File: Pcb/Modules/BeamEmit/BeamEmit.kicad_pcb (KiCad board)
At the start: 2 copper layers, 50.8 x 20.3 mm, 14 parts, among them J1 JACK_RJ45, Q1 Q_NMOS_GSD, X1 HOLE, X2 HOLE, X3 HOLE, X4 HOLE

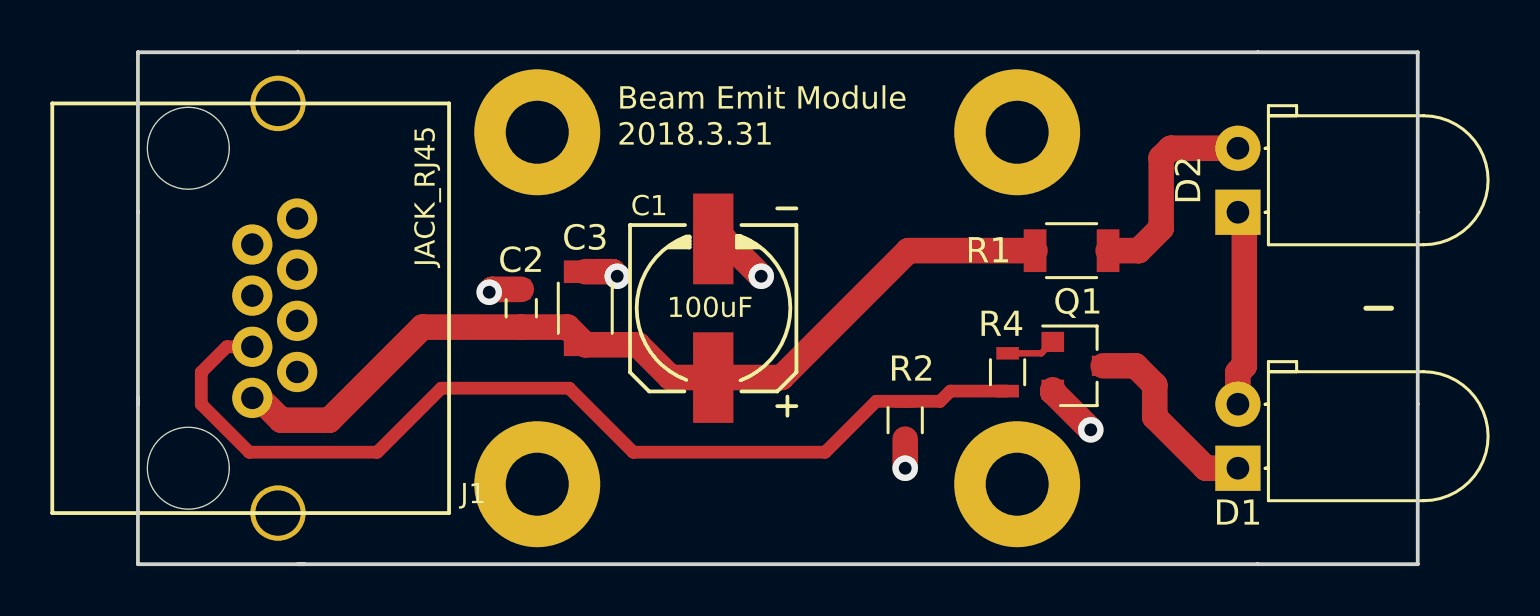
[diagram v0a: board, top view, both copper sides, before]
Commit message: Update module pcbs to fix minor issues and round corners
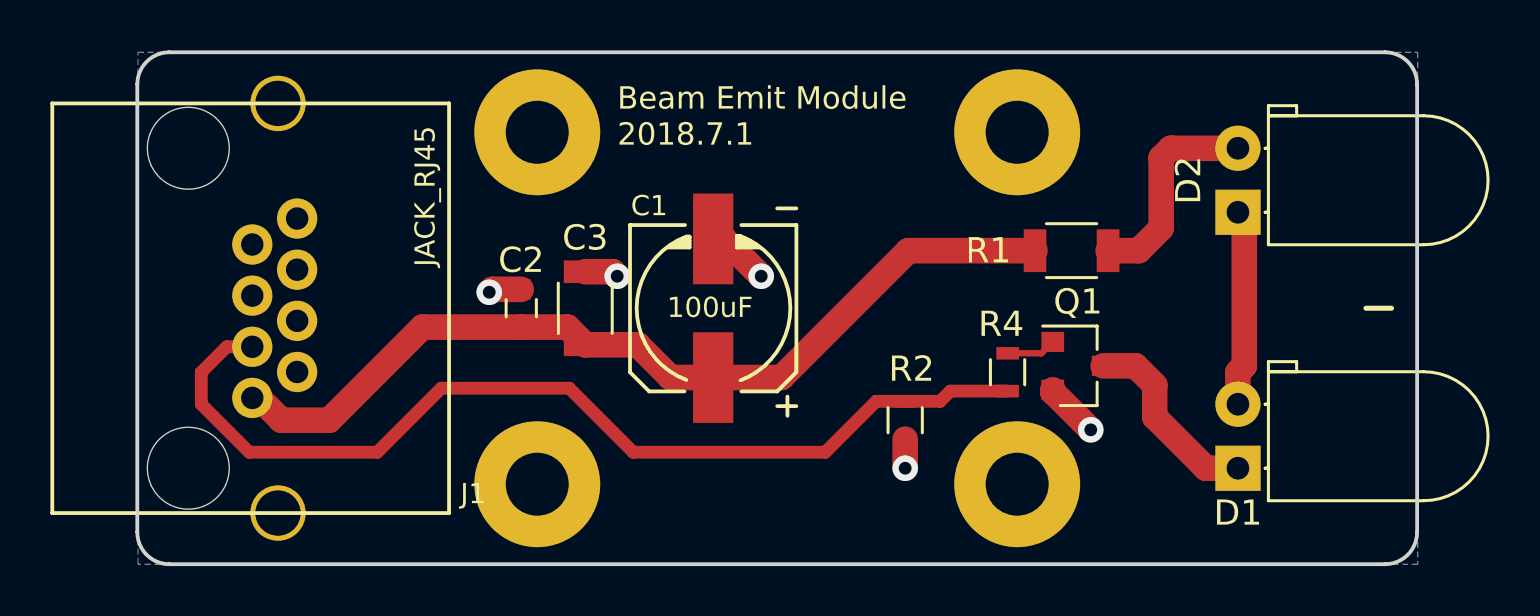
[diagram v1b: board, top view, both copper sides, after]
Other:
- outline, holes or cut-outs redrawn
- board text added: "Beam Emit Module 2018.7.1"
- board text removed: "Beam Emit Module 2018.3.31"
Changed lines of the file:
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@@
     (area 31.906869 34.2568 91.2562 57.2832)
     (thickness 1.6)
-    (drawings 14)
+    (drawings 10)
     (tracks 60)
     (zones 0)
@@
   )
   (setup
-    (last_trace_width 1.016)
+    (last_trace_width 0.254)
     (user_trace_width 0.381)
     (user_trace_width 0.508)
@@
       (net 6 +3V3))
   )
+  (gr_line (start 35.56 54.61) (end 35.56 36.83) (angle 90) (layer Edge.Cuts) (width 0.15))
+  (gr_line (start 85.09 55.88) (end 36.83 55.88) (angle 90) (layer Edge.Cuts) (width 0.15))
+  (gr_line (start 86.36 36.83) (end 86.36 54.61) (angle 90) (layer Edge.Cuts) (width 0.15))
+  (gr_line (start 36.83 35.56) (end 85.09 35.56) (angle 90) (layer Edge.Cuts) (width 0.15))
+  (gr_arc (start 36.83 36.83) (end 35.56 36.83) (angle 90) (layer Edge.Cuts) (width 0.15))
+  (gr_arc (start 36.83 54.61) (end 36.83 55.88) (angle 90) (layer Edge.Cuts) (width 0.15))
+  (gr_arc (start 85.09 54.61) (end 86.36 54.61) (angle 90) (layer Edge.Cuts) (width 0.15))
+  (gr_arc (start 85.09 36.83) (end 85.09 35.56) (angle 90) (layer Edge.Cuts) (width 0.15))
   (gr_line (start 84.328 45.72) (end 85.344 45.72) (angle 90) (layer F.SilkS) (width 0.2))
-  (gr_line (start 86.3854 35.56) (end 86.3854 41.91) (angle 90) (layer Edge.Cuts) (width 0.15))
-  (gr_line (start 80.0354 35.56) (end 86.3854 35.56) (angle 90) (layer Edge.Cuts) (width 0.15))
-  (gr_line (start 86.3854 55.88) (end 80.0354 55.88) (angle 90) (layer Edge.Cuts) (width 0.15))
-  (gr_line (start 86.3854 49.53) (end 86.3854 55.88) (angle 90) (layer Edge.Cuts) (width 0.15))
-  (gr_line (start 35.5854 35.56) (end 35.5854 41.91) (angle 90) (layer Edge.Cuts) (width 0.15))
-  (gr_line (start 41.9354 35.56) (end 35.5854 35.56) (angle 90) (layer Edge.Cuts) (width 0.15))
-  (gr_line (start 35.5854 55.88) (end 35.5854 49.276) (angle 90) (layer Edge.Cuts) (width 0.15))
-  (gr_line (start 42.1894 55.88) (end 35.5854 55.88) (angle 90) (layer Edge.Cuts) (width 0.15))
-  (gr_line (start 35.5854 41.91) (end 35.5854 49.53) (angle 90) (layer Edge.Cuts) (width 0.15))
-  (gr_line (start 86.3854 41.91) (end 86.3854 49.53) (angle 90) (layer Edge.Cuts) (width 0.15))
-  (gr_text "Beam Emit Module\n2018.3.31" (at 54.61 38.1) (layer F.SilkS)
+  (gr_text "Beam Emit Module\n2018.7.1" (at 54.61 38.1) (layer F.SilkS)
     (effects (font (size 0.889 0.889) (thickness 0.2032)) (justify left))
   )
-  (gr_line (start 80.0354 55.88) (end 41.9354 55.88) (angle 90) (layer Edge.Cuts) (width 0.15))
-  (gr_line (start 41.9354 35.56) (end 80.0354 35.56) (angle 90) (layer Edge.Cuts) (width 0.15))
   (segment (start 70.104 47.51) (end 71.444 47.51) (width 0.254) (layer F.Cu) (net 1) (status 10))
   (segment (start 71.444 47.51) (end 71.898 47.056) (width 0.254) (layer F.Cu) (net 1) (status 20))
